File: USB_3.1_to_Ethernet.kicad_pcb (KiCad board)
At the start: 4 copper layers, 77.2 x 25 mm, 79 parts, among them J1 RJ45_JK0654219, J2 USB3_A, U1 LAN7801_9JX, U2 93LC56B_SN, U4 TLV76733, U5 USBLC6-2P6, U6 TPS7A0212, U7 KSZ9031RNXCC, Y1 25MHz, Y2 25MHz

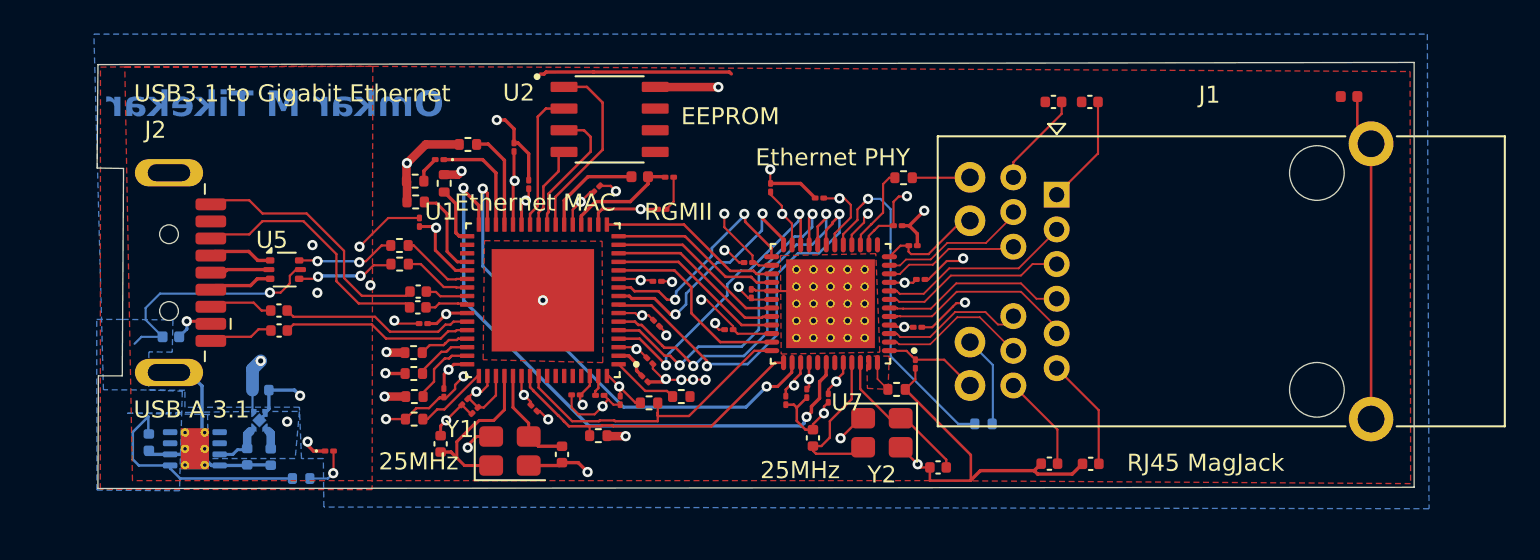
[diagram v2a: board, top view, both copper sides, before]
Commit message: DRC cleared to 0 errors
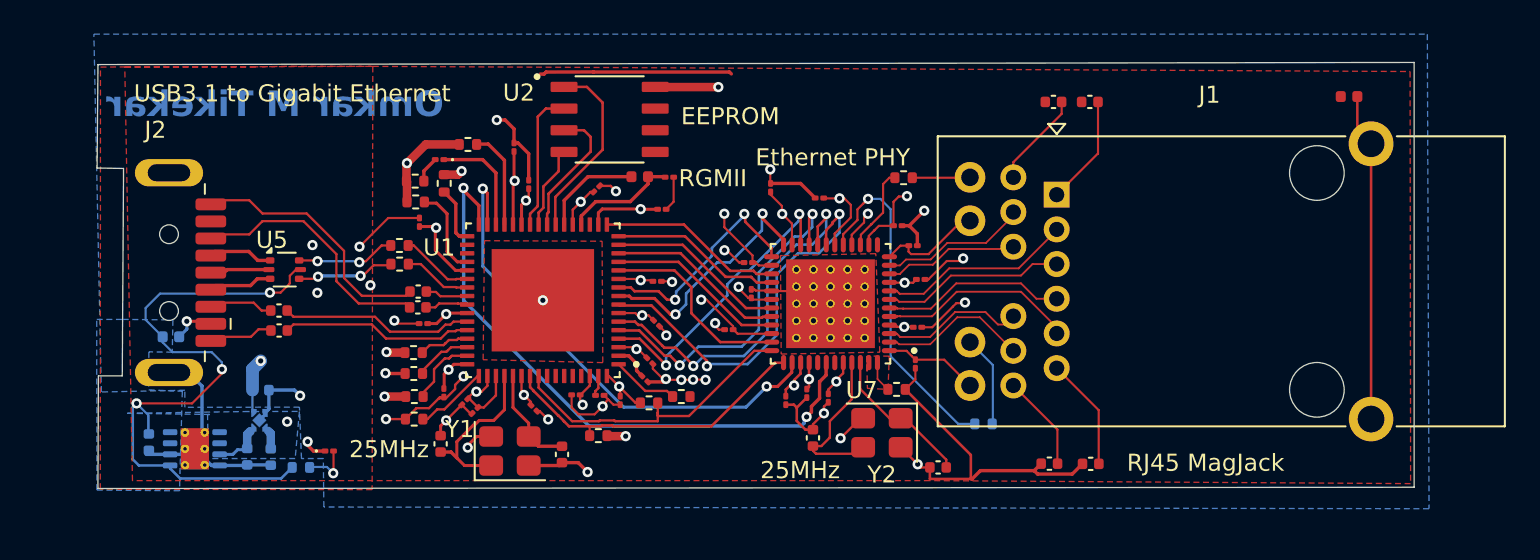
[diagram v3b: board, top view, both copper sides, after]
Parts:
- moved R26 0.65 mm to (70.1, 73.8)
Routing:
- net +5V: track 27.9 -> 38.6 mm, vias 1 -> 3
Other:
- board text removed: "Ethernet MAC"
- board text removed: "USB A 3.1"
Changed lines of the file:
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@@
 		(at 84.299999 63.96 180)
 		(property "Reference" "U1"
-			(at 5.989999 5.19 0)
+			(at 6.074999 3.085 0)
 			(layer "F.SilkS")
 			(effects
@@
 		(at 101.15 64.16 180)
 		(property "Reference" "U7"
-			(at -0.975 -5.785 0)
+			(at -1.825 -5.065 0)
 			(layer "F.SilkS")
 			(effects
@@
 			(at 0.116 1.1032 0)
 			(layer "B.SilkS")
+			(hide yes)
 			(effects
 				(font
@@
 	(footprint "Resistor_SMD:R_0402_1005Metric"
 		(layer "B.Cu")
-		(at 70.14 74.4 180)
+		(at 70.125 73.75 180)
 		(descr "Resistor SMD 0402 (1005 Metric), square (rectangular) end terminal, IPC-7351 nominal, (Body size source: IPC-SM-782 page 72, https://www.pcb-3d.com/wordpress/wp-content/uploads/ipc-sm-782a_amendment_1_and_2.pdf)")
 		(tags "resistor")
@@
 		)
 	)
-	(gr_text "USB A 3.1"
-		(at 60.32 70.95 0)
-		(layer "F.SilkS")
-		(effects
-			(font
-				(size 1 1)
-				(thickness 0.1)
-			)
-			(justify left bottom)
-		)
-	)
 	(gr_text "USB3.1 to Gigabit Ethernet"
 		(at 60.34 52.43 0)
@@
 	)
 	(gr_text "25MHz"
-		(at 74.68 73.99 0)
-		(layer "F.SilkS")
-		(effects
-			(font
-				(size 1 1)
-				(thickness 0.1)
-			)
-			(justify left bottom)
-		)
-	)
-	(gr_text "Ethernet MAC"
-		(at 79.12 58.83 0)
+		(at 72.95 73.275 0)
 		(layer "F.SilkS")
 		(effects
@@
 	)
 	(gr_text "RGMII"
-		(at 90.23 59.37 0)
+		(at 92.25 57.4 0)
 		(layer "F.SilkS")
 		(effects
@@
 	)
 	(segment
-		(start 109.37 73.02)
-		(end 109.37 74.5238)
-		(width 0.1524)
-		(layer "F.Cu")
-		(net "GND")
-	)
-	(segment
 		(start 91.96 58.19)
 		(end 91.96 56.75)
@@
 	)
 	(segment
-		(start 105.53 69.18)
-		(end 109.37 73.02)
-		(width 0.1524)
-		(layer "F.Cu")
-		(net "GND")
-	)
-	(segment
 		(start 91.52 58.63)
 		(end 91.96 58.19)
@@
 	)
 	(segment
-		(start 109.37 74.5238)
-		(end 106.97 74.5238)
+		(start 109.37 73.02)
+		(end 109.37 74.425)
 		(width 0.1524)
 		(layer "F.Cu")
@@
 	)
 	(segment
-		(start 109.93 73.94)
-		(end 109.37 74.5)
-		(width 0.2)
-		(layer "F.Cu")
-		(net "GND")
-	)
-	(segment
 		(start 95.229942 50.589942)
 		(end 95.34 50.7)
@@
 	)
 	(segment
-		(start 113.08 73.94)
-		(end 109.93 73.94)
-		(width 0.2)
-		(layer "F.Cu")
-		(net "GND")
-	)
-	(segment
 		(start 97.66 63.39)
 		(end 97.69 63.42)
@@
 	)
 	(segment
+		(start 105.53 69.18)
+		(end 109.37 73.02)
+		(width 0.1524)
+		(layer "F.Cu")
+		(net "GND")
+	)
+	(segment
 		(start 106.879999 62.74)
 		(end 107.959999 61.66)
@@
 	)
 	(segment
+		(start 113.08 73.94)
+		(end 109.93 73.94)
+		(width 0.2)
+		(layer "F.Cu")
+		(net "GND")
+	)
+	(segment
 		(start 70.52 72.45)
 		(end 70.52 72.24)
@@
 	)
 	(segment
+		(start 109.37 74.425)
+		(end 106.97 74.425)
+		(width 0.1524)
+		(layer "F.Cu")
+		(net "GND")
+	)
+	(segment
 		(start 94.39187 65.29813)
 		(end 94.39187 65.46187)
@@
 	)
 	(segment
+		(start 106.97 74.425)
+		(end 106.97 73.75)
+		(width 0.1524)
+		(layer "F.Cu")
+		(net "GND")
+	)
+	(segment
 		(start 87.885 69.53)
 		(end 88.1275 69.7725)
@@
 	)
 	(segment
+		(start 109.93 73.94)
+		(end 109.445 74.425)
+		(width 0.2)
+		(layer "F.Cu")
+		(net "GND")
+	)
+	(segment
 		(start 79.16 68.91411)
 		(end 79.16 69.16)
@@
 	)
 	(segment
+		(start 109.445 74.425)
+		(end 109.37 74.425)
+		(width 0.2)
+		(layer "F.Cu")
+		(net "GND")
+	)
+	(segment
 		(start 99.173344 71.028476)
 		(end 99.684868 71.54)
@@
 	)
 	(segment
-		(start 106.97 74.5238)
-		(end 106.97 73.75)
-		(width 0.1524)
-		(layer "F.Cu")
-		(net "GND")
-	)
-	(segment
 		(start 77.07 59.14)
 		(end 75.24 59.14)
@@
 	)
 	(segment
-		(start 71.71 74.4)
+		(start 70.66 73.725)
+		(end 71.655 73.725)
+		(width 0.127)
+		(layer "B.Cu")
+		(net "Net-(D2-A)")
+	)
+	(segment
+		(start 71.655 73.725)
 		(end 72.02 74.09)
 		(width 0.127)
@@
 	)
 	(segment
-		(start 70.65 74.4)
-		(end 71.71 74.4)
+		(start 70.635 73.75)
+		(end 70.66 73.725)
 		(width 0.127)
 		(layer "B.Cu")
@@
 	)
 	(segment
+		(start 65.5 68)
+		(end 65.5 68.25)
+		(width 0.127)
+		(layer "F.Cu")
+		(net "+5V")
+	)
+	(segment
 		(start 69.475 62.525)
 		(end 69.8375 62.1625)
@@
 	)
 	(segment
+		(start 65.5 68.25)
+		(end 63.75 70)
+		(width 0.127)
+		(layer "F.Cu")
+		(net "+5V")
+	)
+	(segment
+		(start 63.75 70)
+		(end 60.5 70)
+		(width 0.127)
+		(layer "F.Cu")
+		(net "+5V")
+	)
+	(segment
 		(start 69.475 62.975)
 		(end 69.475 62.525)
@@
 	)
 	(via
+		(at 60.5 70)
+		(size 0.6)
+		(drill 0.3)
+		(layers "F.Cu" "B.Cu")
+		(net "+5V")
+	)
+	(via
 		(at 68.31 63.51)
 		(size 0.6)
@@
 		(net "+5V")
 	)
+	(via
+		(at 65.5 68)
+		(size 0.6)
+		(drill 0.3)
+		(layers "F.Cu" "B.Cu")
+		(net "+5V")
+	)
+	(segment
+		(start 60.635 73.635)
+		(end 62.465 73.635)
+		(width 0.1524)
+		(layer "B.Cu")
+		(net "+5V")
+	)
+	(segment
+		(start 62.465 73.809999)
+		(end 63.055001 74.4)
+		(width 0.1524)
+		(layer "B.Cu")
+		(net "+5V")
+	)
 	(segment
 		(start 62.465 73.635)
@@
 	)
 	(segment
-		(start 62.025 66.1)
-		(end 60.79 66.1)
+		(start 64.9 67)
+		(end 62.605001 67)
 		(width 0.127)
 		(layer "B.Cu")
@@
 	)
 	(segment
-		(start 60.2762 71.6838)
+		(start 65.5 68)
+		(end 65.5 67.6)
+		(width 0.127)
+		(layer "B.Cu")
+		(net "+5V")
+	)
+	(segment
+		(start 65.5 67.6)
+		(end 64.9 67)
+		(width 0.127)
+		(layer "B.Cu")
+		(net "+5V")
+	)
+	(segment
+		(start 60.2762 70.2238)
 		(end 60.2762 73.2762)
 		(width 0.1524)
@@
 	)
 	(segment
-		(start 60.79 66.1)
-		(end 60.38 66.51)
-		(width 0.127)
+		(start 60.2762 73.2762)
+		(end 60.635 73.635)
+		(width 0.1524)
+		(layer "B.Cu")
+		(net "+5V")
+	)
+	(segment
+		(start 68.965 74.4)
+		(end 69.615 73.75)
+		(width 0.1524)
 		(layer "B.Cu")
 		(net "+5V")
@@
 	)
 	(segment
+		(start 63.055001 74.4)
+		(end 68.965 74.4)
+		(width 0.1524)
+		(layer "B.Cu")
+		(net "+5V")
+	)
+	(segment
 		(start 61.87 63.57)
 		(end 68.2 63.57)
@@
 	)
 	(segment
-		(start 63.055001 74.4)
-		(end 69.63 74.4)
-		(width 0.1524)
+		(start 60.5 70)
+		(end 61.19 70.69)
+		(width 0.127)
 		(layer "B.Cu")
 		(net "+5V")
 	)
 	(segment
-		(start 60.635 73.635)
-		(end 62.465 73.635)
-		(width 0.1524)
+		(start 61.19 70.69)
+		(end 61.19 70.77)
+		(width 0.127)
 		(layer "B.Cu")
 		(net "+5V")
 	)
 	(segment
-		(start 60.2762 73.2762)
-		(end 60.635 73.635)
+		(start 60.5 70)
+		(end 60.2762 70.2238)
 		(width 0.1524)
 		(layer "B.Cu")
@@
 	)
 	(segment
-		(start 61.19 70.77)
-		(end 60.2762 71.6838)
-		(width 0.1524)
+		(start 62.605001 67)
+		(end 62.025 66.419999)
+		(width 0.127)
+		(layer "B.Cu")
+		(net "+5V")
+	)
+	(segment
+		(start 62.025 66.419999)
+		(end 62.025 66.1)
+		(width 0.127)
 		(layer "B.Cu")
 		(net "+5V")
@@
 	)
 	(segment
-		(start 62.465 73.809999)
-		(end 63.055001 74.4)
-		(width 0.1524)
-		(layer "B.Cu")
-		(net "+5V")
-	)
-	(segment
 		(start 61.03 65.105)
 		(end 61.03 64.41)
@@
 			(pts
 				(xy 59.69 65.08) (xy 62.63 65.11) (xy 62.59 67) (xy 61.22 66.98) (xy 61.21 69.21) (xy 63.18 69.29)
-				(xy 63.03 74.51) (xy 63.02 75.12) (xy 58.174992 75.076351) (xy 58.165005 65.08)
+				(xy 63.03 74.51) (xy 63.02 75.12) (xy 58.175013 75.075586) (xy 58.165027 65.080766)
 			)
 		)
@@
 			(pts
 				(xy 58 48.37) (xy 136.11 48.37) (xy 136.21 76.17) (xy 71.47 76.07) (xy 71.44 73.23) (xy 70.16 73.23)
-				(xy 70.04 70.22) (xy 63.33 70.23) (xy 63.33 69.23) (xy 58.56 69.2)
+				(xy 70.04 70.22) (xy 63.33 70.23) (xy 63.33 69.23) (xy 58.435894 69.331772)
 			)
 		)

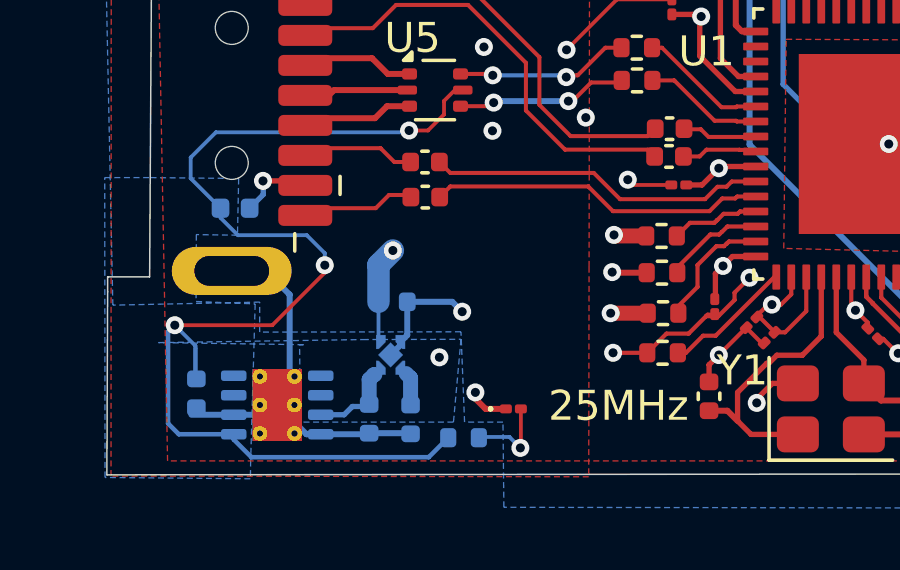
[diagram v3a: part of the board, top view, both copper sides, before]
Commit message: Step files added for ics
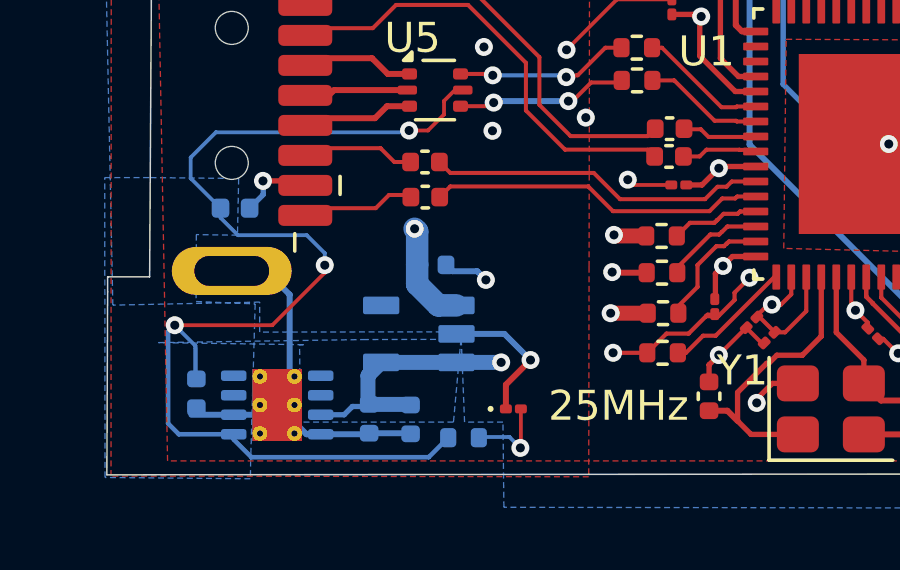
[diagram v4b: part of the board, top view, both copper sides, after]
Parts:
- U6: footprint TPS7A0230PDQNR:IC_TPS7A0230PDQNR -> TPS7A0212:Tps_7a0212
- moved C2 1.78 mm to (69.1, 68.0)
- moved U6 1.17 mm to (68.6, 70.3), turned to 180 degrees
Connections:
- C48 pad 1: 1v2_core -> 3v3_out
- R23 pad 1: Net-(U7-ISET) -> Net-(U3-ISET)
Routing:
- net 3v3_out: track 125.9 -> 128.6 mm
- net GND: track 123.6 -> 124.6 mm
- net 1v2_core: track 133.1 -> 132.3 mm

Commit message: Datasheets for all the ICs added iin the Docs folder
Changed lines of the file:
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@@
 	)
 	(gr_text "RGMII"
-		(at 92.25 57.4 0)
+		(at 91.68 73.54 0)
 		(layer "F.SilkS")
 		(effects

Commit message: resolved drc errors of shorting nets
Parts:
- removed U7: KSZ9031RNXCC, KSZ9031RNXCC:IC_KSZ9031RNXCC
- added U3: KSZ9031RNXCC, KSZ9031RNXCC:IC_KSZ9031RNXCC, F.Cu at (101.2, 64.2)
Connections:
- C48 pad 1: 3v3_out -> 1v2_core
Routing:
- net Net-(U7-ISET): track 1.82 -> 0.00 mm
- net Net-(U3-ISET): track 0.00 -> 1.82 mm

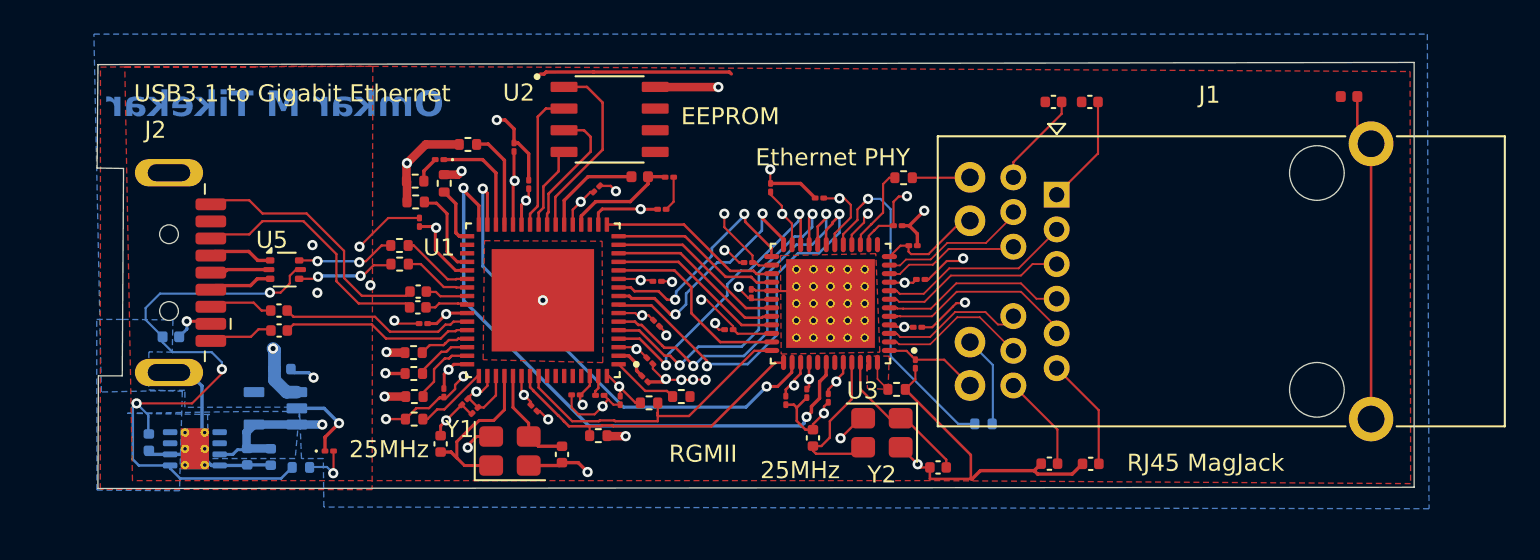
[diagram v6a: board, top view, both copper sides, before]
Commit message: open gnd vias controlled pour spillage and improved clck circuitry
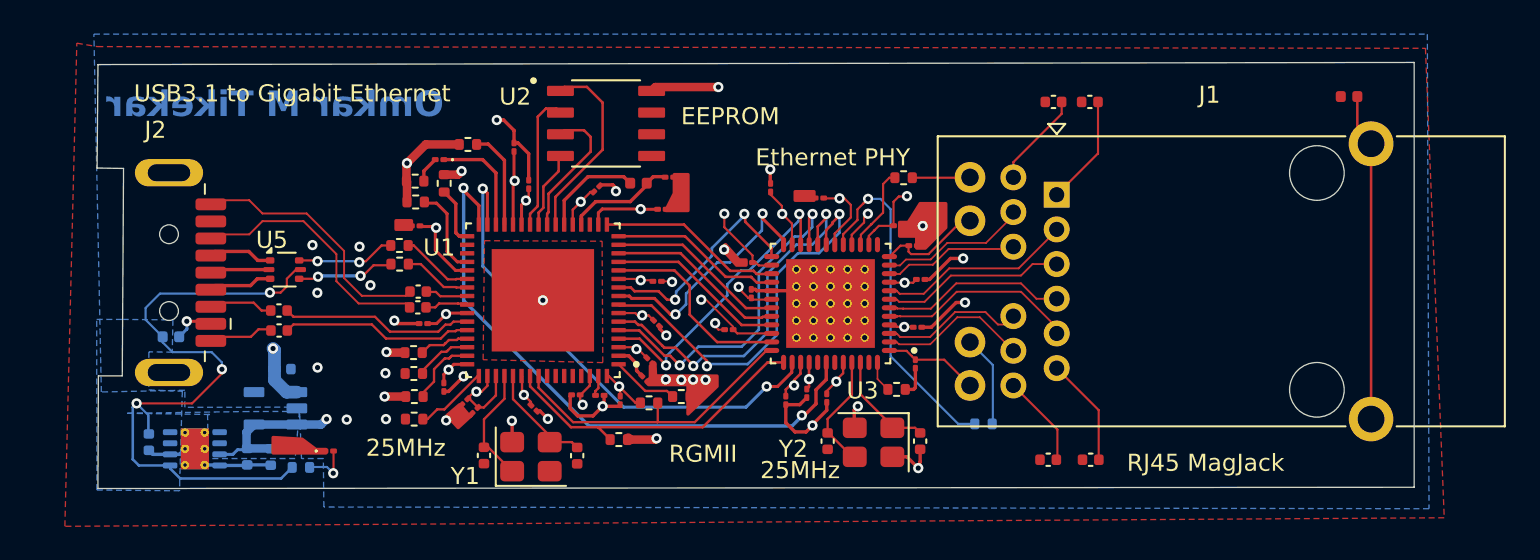
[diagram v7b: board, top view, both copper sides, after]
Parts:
- moved C5 2.63 mm to (80.8, 73.0), turned to -90 degrees
- moved C7 1.86 mm to (106.4, 72.2), turned to -90 degrees
- moved Y1 1.27 mm to (83.6, 73.1)
- moved R3 1.22 mm to (88.8, 72.1)
- moved C6 0.89 mm to (86.3, 73.1)
- moved C8 0.88 mm to (101.0, 72.2), turned to 90 degrees
- moved Y2 0.74 mm to (103.7, 72.3)
- moved L1 0.39 mm to (89.9, 57.1)
- moved C18 0.33 mm to (78.5, 69.0)
- moved U2 0.32 mm to (88.0, 53.6)
- moved C29 0.30 mm to (76.8, 59.6), turned to 180 degrees
- moved C13 0.24 mm to (113.9, 73.3)
- moved C14 0.24 mm to (116.4, 73.3)
- moved C45 0.09 mm to (100.9, 69.7)
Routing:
- net GND: track 124.6 -> 49.5 mm, vias 33 -> 32
- net /XI_LAN: track 9.78 -> 6.90 mm
- net 3v3_out: track 128.6 -> 131.4 mm
- net /XO_PHY: track 9.55 -> 6.90 mm
- net /XI_PHY: track 8.74 -> 6.36 mm

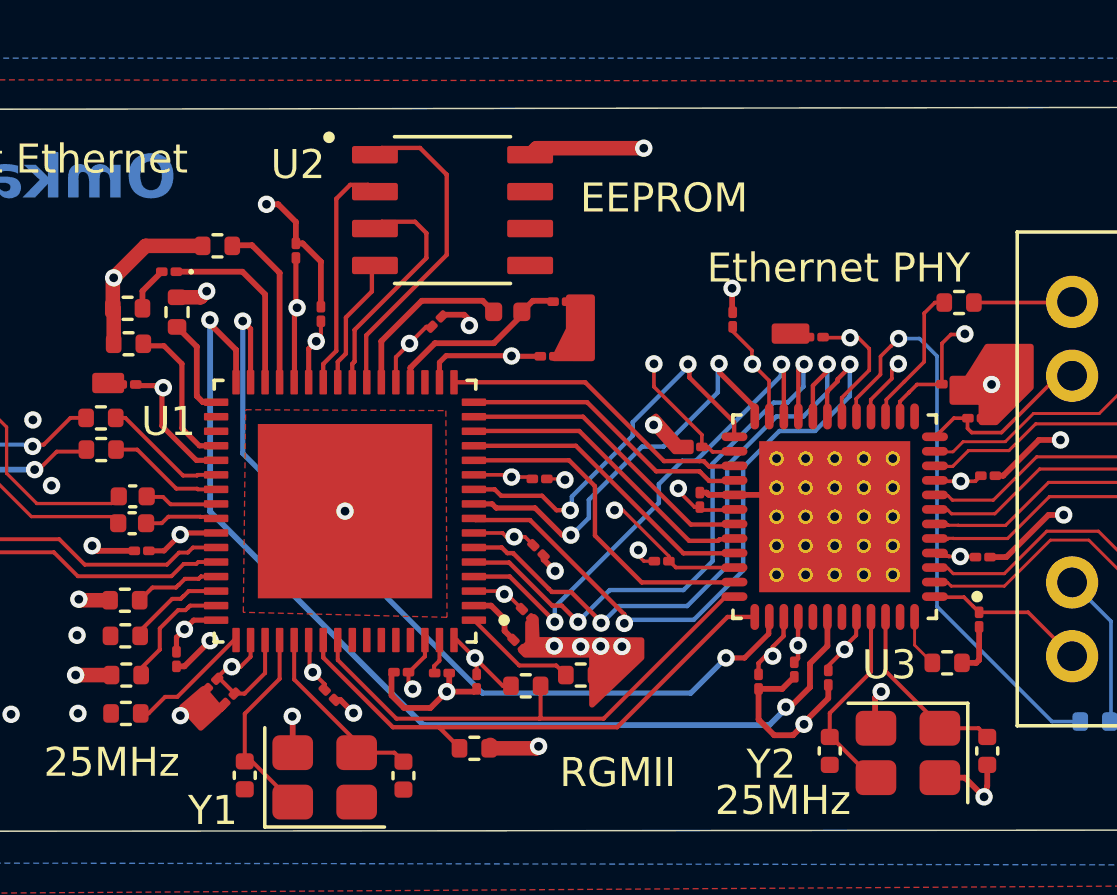
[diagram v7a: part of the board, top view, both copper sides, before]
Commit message: added gnd stitching vias near rgmii interface for short return current loop
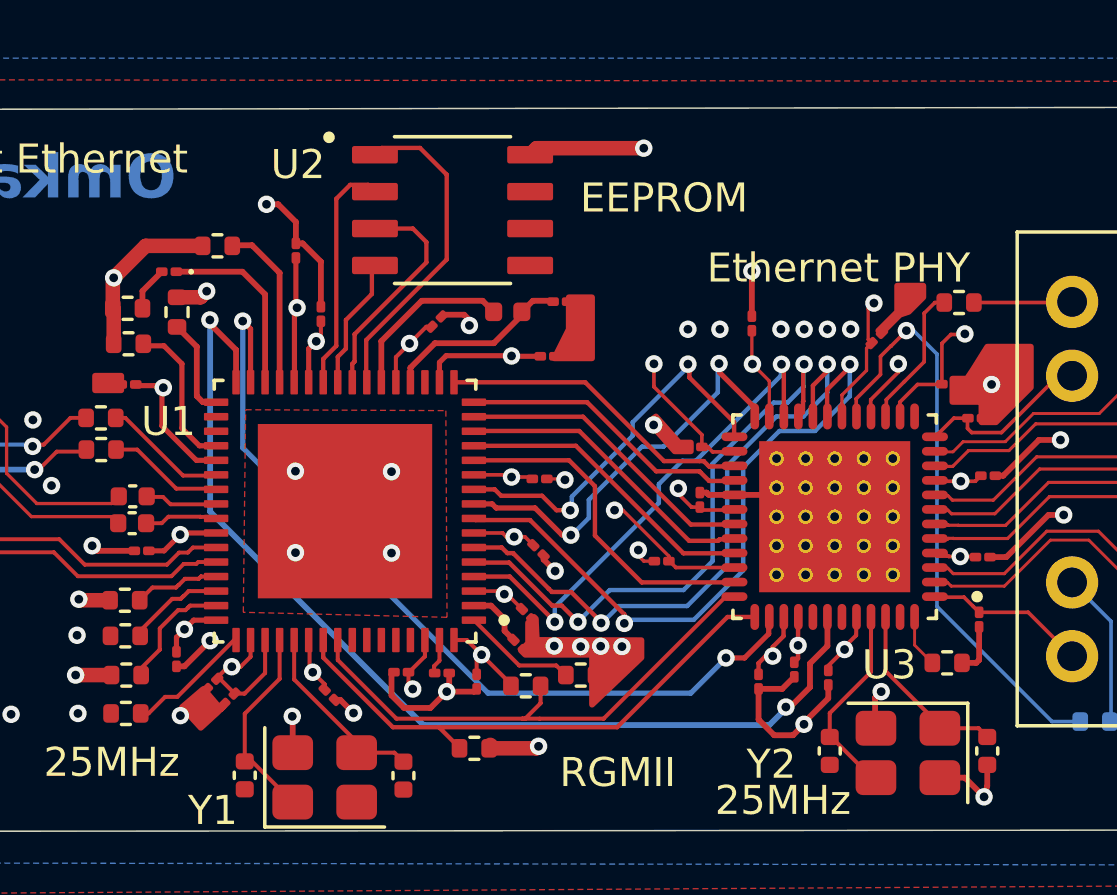
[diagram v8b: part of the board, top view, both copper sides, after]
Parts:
- moved C31 2.10 mm to (102.6, 58.0), turned to 45 degrees
- moved C42 0.67 mm to (98.3, 57.5)
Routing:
- net GND: track 49.5 -> 50.2 mm, vias 32 -> 41
